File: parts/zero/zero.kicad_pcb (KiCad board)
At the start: 2 copper layers, 38.4 x 21.6 mm, 12 parts, among them J1 Conn_02x02_Odd_Even, J2 Conn_02x04_Odd_Even, J3 Conn_01x02, K1 HK19F

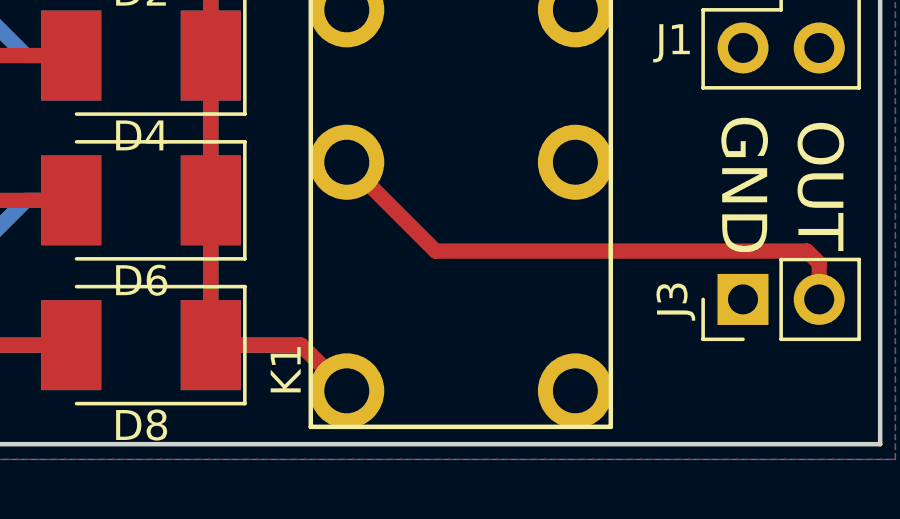
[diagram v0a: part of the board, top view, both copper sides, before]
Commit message: Add flyback diode to zero.
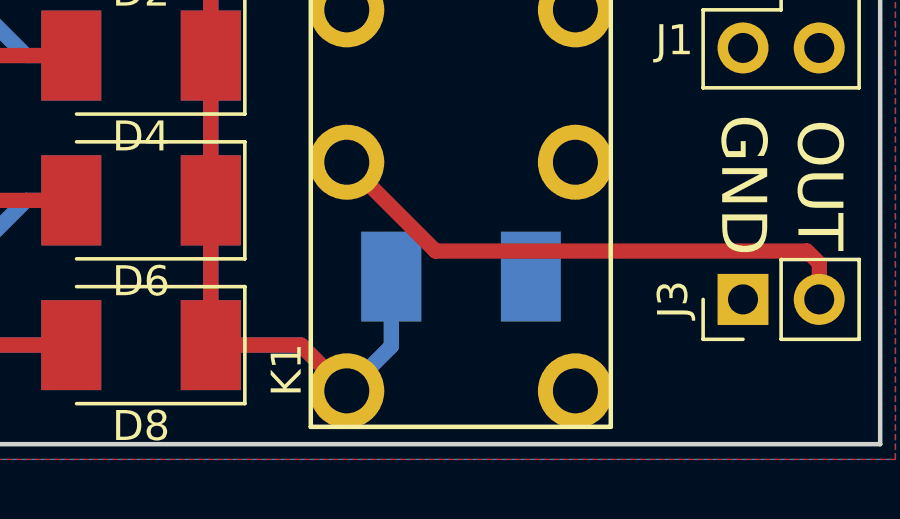
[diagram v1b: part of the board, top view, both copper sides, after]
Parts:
- added D9: D, Diodes_SMD:D_2114, B.Cu at (162.3, 109.0)
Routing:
- net Net-(D1-Pad1): track 39.3 -> 43.7 mm
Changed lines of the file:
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@@
     (thickness 1.6)
     (drawings 12)
-    (tracks 48)
+    (tracks 50)
     (zones 0)
-    (modules 12)
+    (modules 13)
     (nets 13)
   )
@@
     )
   )
+  (module Diodes_SMD:D_2114 (layer B.Cu)
+    (at 162.306 108.966)
+    (descr "Diode SMD 2114, reflow soldering http://datasheets.avx.com/schottky.pdf")
+    (tags "Diode 2114")
+    (attr smd)
+    (fp_text reference D9 (at 0 2.7) (layer B.SilkS)
+      (effects (font (size 1 1) (thickness 0.15)) (justify mirror))
+    )
+    (fp_text value D (at 0 -2.8) (layer B.Fab)
+      (effects (font (size 1 1) (thickness 0.15)) (justify mirror))
+    )
+    (fp_line (start 2.6 -1.8) (end 2.6 1.8) (layer B.Fab) (width 0.1))
+    (fp_line (start 2.6 -1.8) (end -2.6 -1.8) (layer B.Fab) (width 0.1))
+    (fp_line (start -3.46 1.95) (end 2.15 1.95) (layer B.SilkS) (width 0.12))
+    (fp_line (start -3.46 -1.95) (end 2.15 -1.95) (layer B.SilkS) (width 0.12))
+    (fp_line (start -0.64944 -0.00102) (end 0.50118 0.79908) (layer B.Fab) (width 0.1))
+    (fp_line (start -0.64944 -0.00102) (end 0.50118 -0.75032) (layer B.Fab) (width 0.1))
+    (fp_line (start 0.50118 -0.75032) (end 0.50118 0.79908) (layer B.Fab) (width 0.1))
+    (fp_line (start -0.64944 0.79908) (end -0.64944 -0.80112) (layer B.Fab) (width 0.1))
+    (fp_line (start 0.50118 -0.00102) (end 1.4994 -0.00102) (layer B.Fab) (width 0.1))
+    (fp_line (start -0.64944 -0.00102) (end -1.55114 -0.00102) (layer B.Fab) (width 0.1))
+    (fp_line (start -3.61 -2.1) (end -3.61 2.1) (layer B.CrtYd) (width 0.05))
+    (fp_line (start 3.61 -2.1) (end -3.61 -2.1) (layer B.CrtYd) (width 0.05))
+    (fp_line (start 3.61 2.1) (end 3.61 -2.1) (layer B.CrtYd) (width 0.05))
+    (fp_line (start -3.61 2.1) (end 3.61 2.1) (layer B.CrtYd) (width 0.05))
+    (fp_line (start 2.6 1.8) (end -2.6 1.8) (layer B.Fab) (width 0.1))
+    (fp_line (start -2.6 -1.8) (end -2.6 1.8) (layer B.Fab) (width 0.1))
+    (fp_line (start -3.46 1.95) (end -3.46 -1.95) (layer B.SilkS) (width 0.12))
+    (fp_text user %R (at 0 2.7) (layer B.Fab)
+      (effects (font (size 1 1) (thickness 0.15)) (justify mirror))
+    )
+    (pad 2 smd rect (at 2.325 0) (size 2 3) (layers B.Cu B.Paste B.Mask)
+      (net 10 GND))
+    (pad 1 smd rect (at -2.325 0) (size 2 3) (layers B.Cu B.Paste B.Mask)
+      (net 2 "Net-(D1-Pad1)"))
+    (model ${KISYS3DMOD}/Diodes_SMD.3dshapes/D_2114.wrl
+      (at (xyz 0 0 0))
+      (scale (xyz 1 1 1))
+      (rotate (xyz 0 0 0))
+    )
+  )
   (dimension 38.354 (width 0.3) (layer F.SilkS)
     (gr_text "1.5100 in" (at 157.099 121.48) (layer F.SilkS)
@@
   (segment (start 156.972 111.252) (end 158.496 112.776) (width 0.508) (layer F.Cu) (net 2))
   (segment (start 153.963 111.252) (end 156.972 111.252) (width 0.508) (layer F.Cu) (net 2))
+  (segment (start 159.981 111.291) (end 158.496 112.776) (width 0.508) (layer B.Cu) (net 2))
+  (segment (start 159.981 108.966) (end 159.981 111.291) (width 0.508) (layer B.Cu) (net 2))
   (segment (start 146.304 96.774) (end 142.748 100.33) (width 0.508) (layer F.Cu) (net 3))
   (segment (start 149.313 96.774) (end 146.304 96.774) (width 0.508) (layer F.Cu) (net 3))

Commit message: Many things happened at 35C3.
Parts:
- J3: value Conn_01x02 -> Conn_02x04_Odd_Even; footprint Pin_Headers:Pin_Header_Straight_1x02_Pitch2.54mm -> Pin_Headers:Pin_Header_Straight_2x04_Pitch2.54mm
- moved J3 5.89 mm to (170.9, 103.9), turned to 0 degrees
- moved J1 3.45 mm to (170.7, 95.5)
- moved D9 1.99 mm to (160.3, 109.0), turned to 180 degrees
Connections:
- J3 pad 2: Net-(J3-Pad2) -> (no net)
- K1 pad 1: Net-(D1-Pad1) -> GND
- K1 pad 16: GND -> Net-(D1-Pad1)
- K1 pad 4: Net-(J3-Pad2) -> Net-(J3-Pad6)
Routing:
- net Net-(D1-Pad2): track 11.8 -> 53.9 mm
- net Net-(D8-Pad2): track 7.93 -> 44.1 mm, vias 0 -> 1
- net Net-(J3-Pad6): track 0.00 -> 25.4 mm
- net Net-(J3-Pad2): track 18.3 -> 0.00 mm
- net Net-(D1-Pad1): track 43.7 -> 42.9 mm, vias 0 -> 5
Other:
- board size 38.4 x 21.6 mm -> 38.9 x 23.1 mm
- board text removed: "+"
- board text removed: "GND"
- board text removed: "OUT"
- board text removed: "PWR"
